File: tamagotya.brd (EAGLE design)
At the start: 27.9 x 31.8 mm, 34 parts, among them U100 ESP32-D2WD, U200 UT-0206-P05FOLDED, U300 4MB Flash, Y100 40Mhz 3.2X2.5

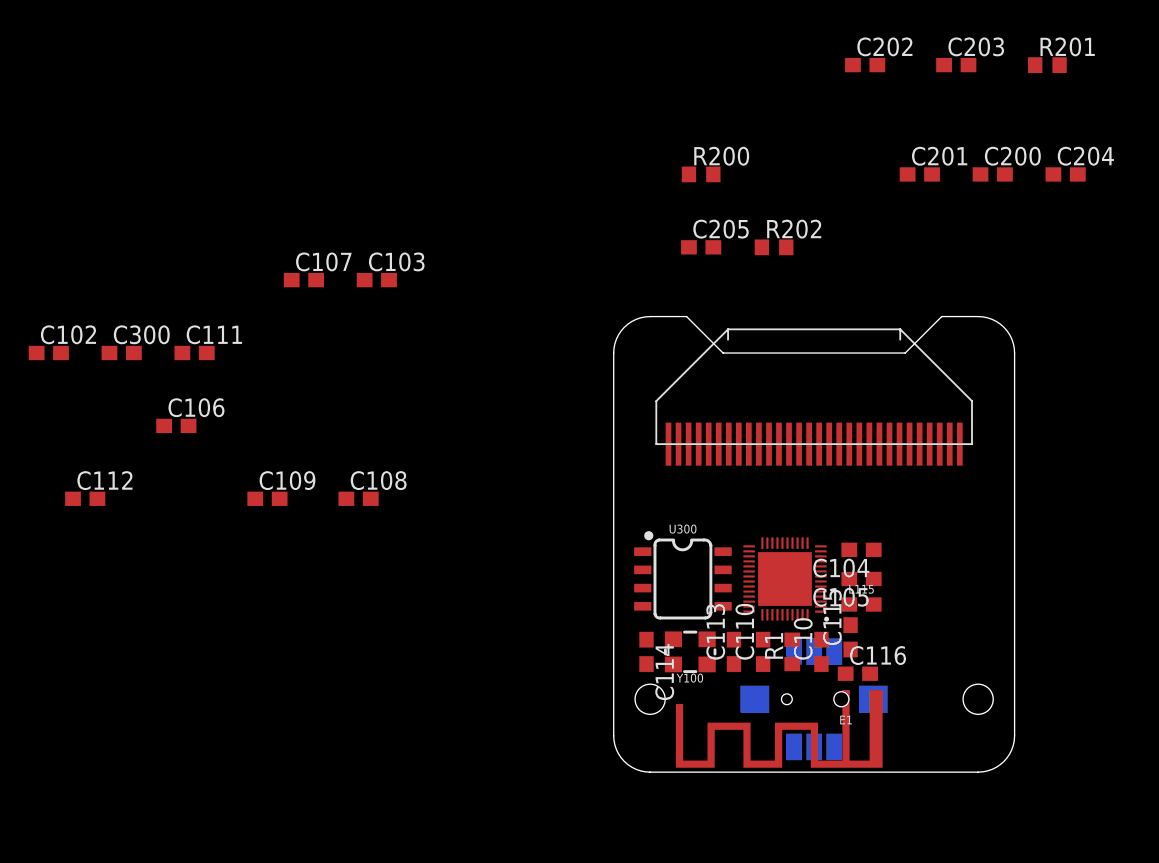
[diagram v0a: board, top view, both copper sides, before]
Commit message: Laid out, need to add charge/boost circuit and its basically done. Could do with a UART too.
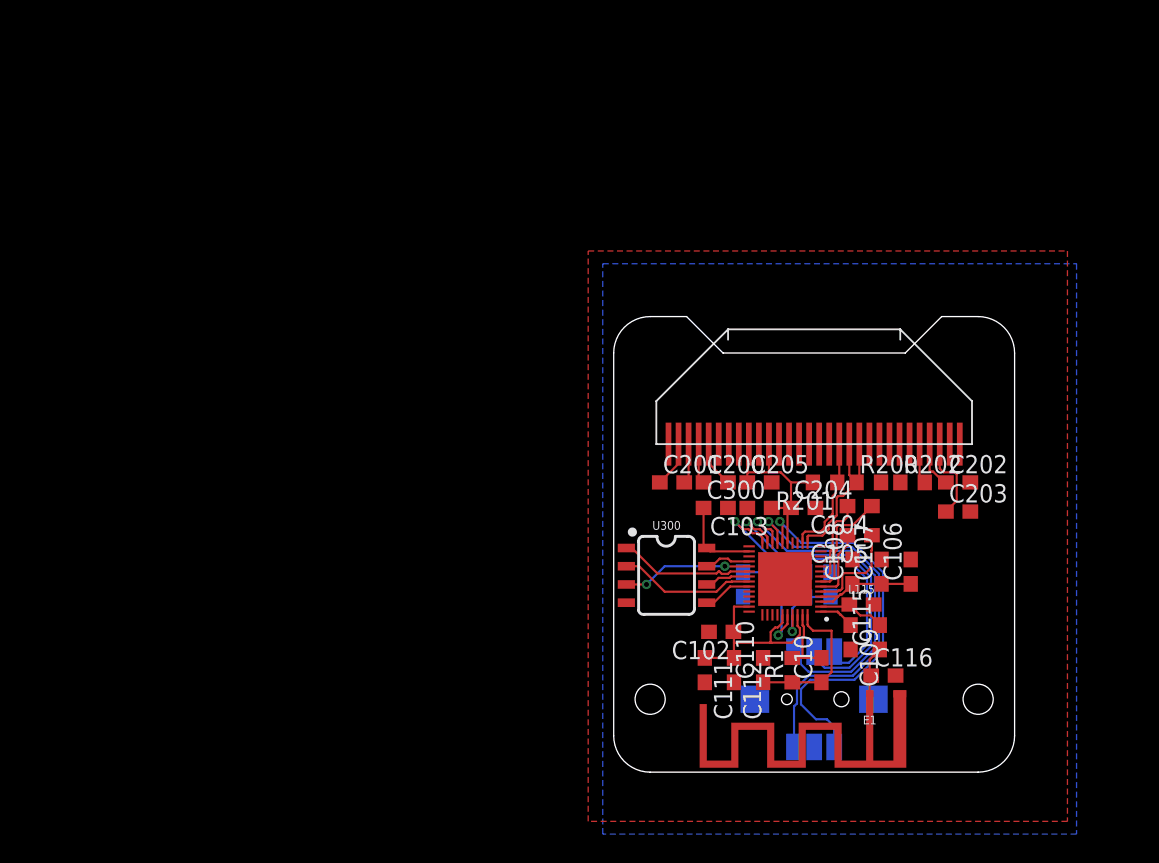
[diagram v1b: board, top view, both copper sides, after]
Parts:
- moved C106 52.2 mm to (20.7, 14.0), turned to 90 degrees
- moved C102 50.7 mm to (7.49, 9.78), turned to 180 degrees
- moved C112 46.8 mm to (8.38, 7.11), turned to 270 degrees
- moved C107 45.1 mm to (18.7, 14.0), turned to 90 degrees
- moved C300 42.8 mm to (7.11, 18.4)
- moved C111 41.9 mm to (6.35, 7.11), turned to 270 degrees
- moved C109 41.8 mm to (16.5, 9.40), turned to 270 degrees
- moved C108 34.8 mm to (16.6, 14.0), turned to 90 degrees
- moved R201 33.0 mm to (14.7, 20.2), turned to 180 degrees
- moved C203 31.1 mm to (24.0, 18.2)
- moved C103 31.0 mm to (10.2, 18.4), turned to 180 degrees
- moved C202 29.8 mm to (24.0, 20.2)
- moved C204 29.6 mm to (13.2, 18.4)
- moved C200 28.9 mm to (7.11, 20.2)
- moved C201 27.5 mm to (4.06, 20.2)
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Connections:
- net N$1 renamed SENSOR_VN
- net N$2 renamed SENSOR_CAPN
- net N$3 renamed SENSOR_VP
- net N$4 renamed SENSOR_CAPP
- net N$8 renamed CAP1
- net N$9 renamed CAP2
- removed net CLICK: JOY.CTR
- removed net DOWN: JOY.D
- removed net GPIO26: U100.15
- removed net GPIO27: U100.16
- removed net LEFT: JOY.C
- removed net RIGHT: JOY.B
- removed net UP: JOY.A
- new net GPIO15: JOY.B, U100.21
- net GPIO0: now also JOY.CTR
- net GPIO13: now also JOY.D
- net GPIO14: no longer U100.21
- net GPIO2: now also JOY.A
- net GPIO4: now also JOY.C
- net SCL: now also U100.16
- net SDA: now also U100.15
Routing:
- net 3.3V: track 0.00 -> 41.0 mm
- net GPIO13: track 0.00 -> 28.0 mm, vias 0 -> 1
- net GPIO15: track 0.00 -> 27.3 mm, vias 0 -> 1
- net GPIO2: track 0.00 -> 24.1 mm, vias 0 -> 1
- net GPIO0: track 0.00 -> 22.8 mm, vias 0 -> 1
- net GPIO4: track 0.00 -> 21.8 mm, vias 0 -> 1
- net SDA: track 0.00 -> 12.1 mm
- net CAP1: track 0.00 -> 10.5 mm
- net SDO/SD0: track 0.00 -> 9.59 mm
- net SCS/CMD: track 0.00 -> 9.49 mm
- net SWP/SD3: track 0.00 -> 9.09 mm, vias 0 -> 2
- net SCL: track 0.00 -> 8.60 mm
- net N$6: track 0.00 -> 8.40 mm, vias 0 -> 1
- net SENSOR_CAPN: track 0.00 -> 7.69 mm
- net SENSOR_VP: track 0.00 -> 7.02 mm
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- added copper zone on layer 1, net GND
- added copper zone on layer 16, net GND
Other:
- board text added: "28mm"
- board text added: "32mm"

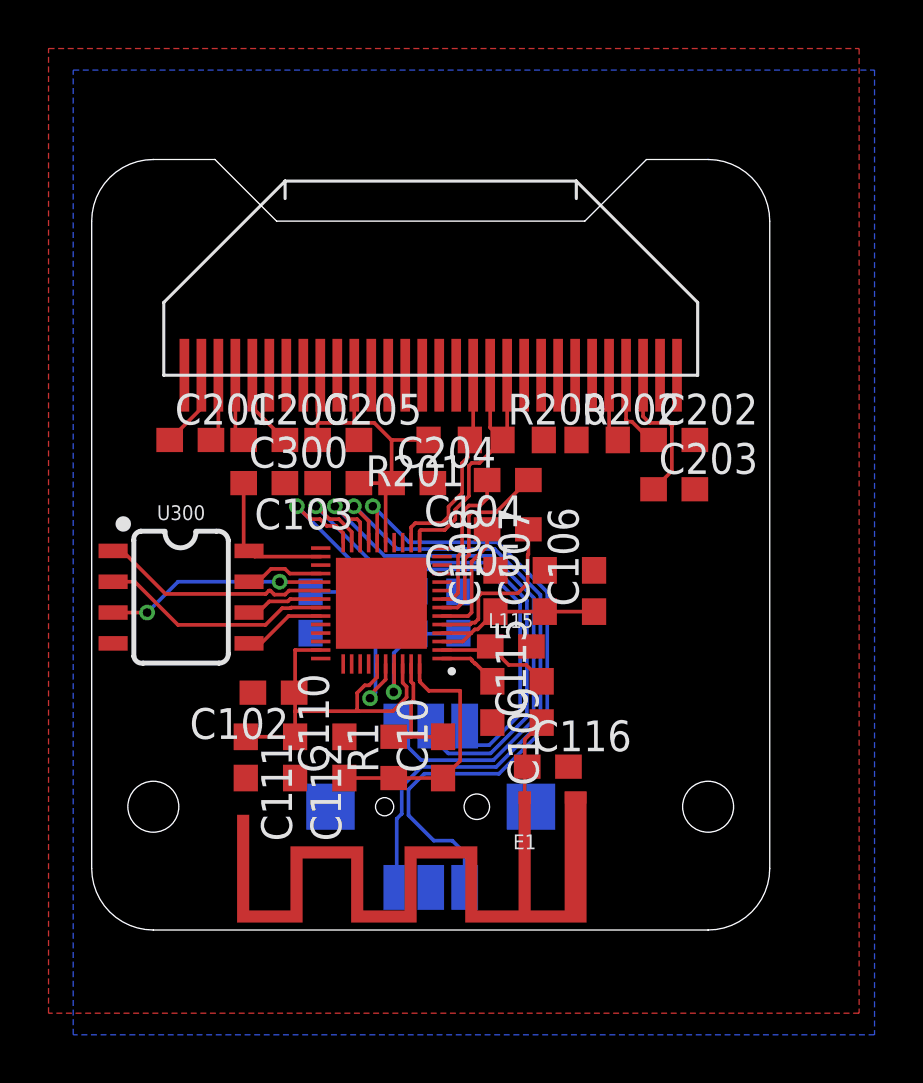
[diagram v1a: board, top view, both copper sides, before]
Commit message: Almost there. Mostly laid out. Just got CP2102 power to resolve.
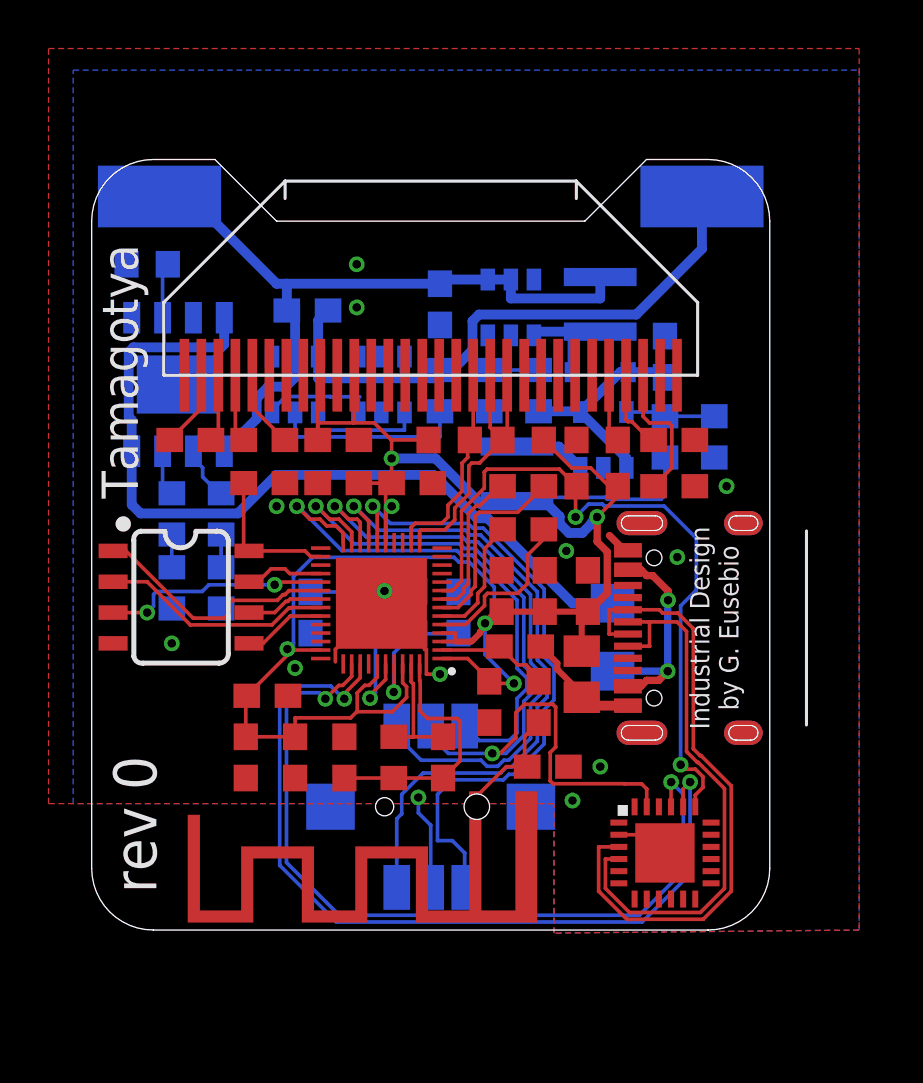
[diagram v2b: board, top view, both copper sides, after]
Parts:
- added C1, C2: 22uH, rcl:C0603
- added C1503: 0.1uF, rcl:C0603
- added C3: 47uF, rcl:C0805
- added D2002: (no value), SparkFun-DiscreteSemi:SOD-323
- added F1: 6V/0.5A, SparkFun-Fuses:1206
- added L2000: 10uH, geusebio:INDUCTOR_3.0X3.0
- added L2100: 4.7uH, geusebio:INDUCTOR_3.0X3.0
- added NEG, POS: (no value), wirepad:SMD2,54-5,08
- added R1001: 1.2k, rcl:R0603
- added R1006, R1007, R1501, R2005, R2103: 1k, rcl:R0603
- added R1008, R1009: 2k, rcl:R0603
- added R2: 10k, rcl:R0603
- added R2004: 7.5k, rcl:R0603
- added R2102: 4.5k, rcl:R0603
- added U$2: USB-C, geusebio:USB_C-XKBENTERPRISEU262-16XN-4BVC11
- added U$3: CP2102N-QFN24, geusebio:QFN24-4X4
- added U1000: TP4056, geusebio:SOP-8
- added U1500: FS312F-G, geusebio:SOT23-6
- added U1550: FS8205, geusebio:SOT23-6
- added U2000: MT3608, geusebio:SOT23-6
- added U2100: M3406, geusebio:SOT23-5
- moved E1 2.03 mm to (15.8, 5.21)
- moved C104 0.68 mm to (17.8, 18.3)
- moved C105 0.64 mm to (17.8, 16.5)
- moved L115 0.38 mm to (17.7, 11.7)
- moved C102 0.28 mm to (7.24, 9.65), turned to 0 degrees
- moved C106 0.25 mm to (20.4, 14.0)
- moved C108 0.25 mm to (16.9, 14.0)
- moved C109 0.13 mm to (16.4, 9.40)
- moved C115 0.13 mm to (18.4, 9.40)
- moved C203 0.13 mm to (24.0, 18.3)
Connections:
- net N$5 renamed XTAL_P
- net N$6 renamed XTAN_N
- removed net CHIP_PU: U100.9
- removed net U0RXD: U100.40
- removed net U0TXD: U100.41
- new net 5V: C2.1, D2002.C, R2004.2, U2100.1, U2100.4
- new net BUCK: D2002.A, L2000.P$2, U2000.1
- new net CHRG: R1006.2, U1000.7
- new net CHRG_3V3: R1006.1, R1008.2
- new net D+: U$2.D+1, U$2.D+2, U$3.3
- new net D-: U$2.D-1, U$2.D-2, U$3.4
- new net FS_CS: R1501.2, U1500.2
- new net GND_BATT: C1503.2, NEG.1, R1501.1, U1500.6, U1550.3
- new net N$17: U$3.5
- new net N$18: U$3.6
- new net N$20: U$3.1
- new net N$21: U$3.24
- new net N$23: U$3.22
- new net N$26: U$3.18
- new net N$27: U$3.17
- new net N$28: U$3.15
- new net N$29: U$3.14
- new net N$3: R2004.1, R2005.2, U2000.3
- new net N$30: U$3.13
- new net N$31: U$3.12
- new net N$32: U$3.11
- new net N$33: U$3.9
- new net N$35: U$3.8
- new net N$36: U$3.7
- new net N$4: R1001.2, U1000.2
- new net N$8: L2100.P$1, U2100.3
- new net N$9: R2102.1, R2103.2, U2100.5
- new net OC: U1500.3, U1550.6
- new net OD: U1500.1, U1550.4
- new net RESET: R2.1, U$3.19, U100.9
- new net STDBY: R1007.2, U1000.6
- new net STDBY_3V3: R1007.1, R1009.2
- new net U100RXD: U$3.21, U100.40
- new net U100TXD: U$3.20, U100.41
- new net V_BATT: C1.1, C1503.1, L2000.P$1, POS.1, U1000.5, U1500.5, U2000.4, U2000.5
- new net V_USB: F1.1, U1000.4, U1000.8
- new net V_USB_UNFUSED: F1.2, U$2.V+1, U$2.V+2
- net 3.3V: now also C3.1, L2100.P$2, R2.2, R2102.2
- net GND: now also C1.2, C2.2, C3.2, R1001.1, R1008.1, R1009.1, R2005.1, R2103.1, U$2.GND1, U$2.GND2, U$3.2, U$3.EXP, U1000.1, U1000.3, U1550.1, U2000.2, U2100.2
- net GPIO0: now also U$3.23
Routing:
- net 3.3V: track 41.0 -> 93.3 mm, vias 0 -> 6
- net U100TXD: track 0.00 -> 35.2 mm, vias 0 -> 2
- net V_USB: track 0.00 -> 34.7 mm
- net U100RXD: track 0.00 -> 33.3 mm, vias 0 -> 2
- net V_BATT: track 0.00 -> 30.7 mm
- net RESET: track 0.00 -> 29.2 mm, vias 0 -> 2
- net D+: track 0.00 -> 26.1 mm
- net GND_BATT: track 0.00 -> 24.9 mm
- net D-: track 0.00 -> 23.5 mm
- net GND: track 0.00 -> 21.4 mm, vias 0 -> 13
- net GPIO0: track 22.8 -> 35.4 mm, vias 1 -> 2
- net V_USB_UNFUSED: track 0.00 -> 9.52 mm, vias 0 -> 2
- net 5V: track 0.00 -> 9.08 mm
- net FS_CS: track 0.00 -> 8.03 mm
- net OD: track 0.00 -> 5.02 mm
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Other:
- board text added: "+"
- board text added: "-"
- board text added: "Industrial Design by G. Eusebio"
- board text added: "Tamagotya"
- board text added: "rev 0"

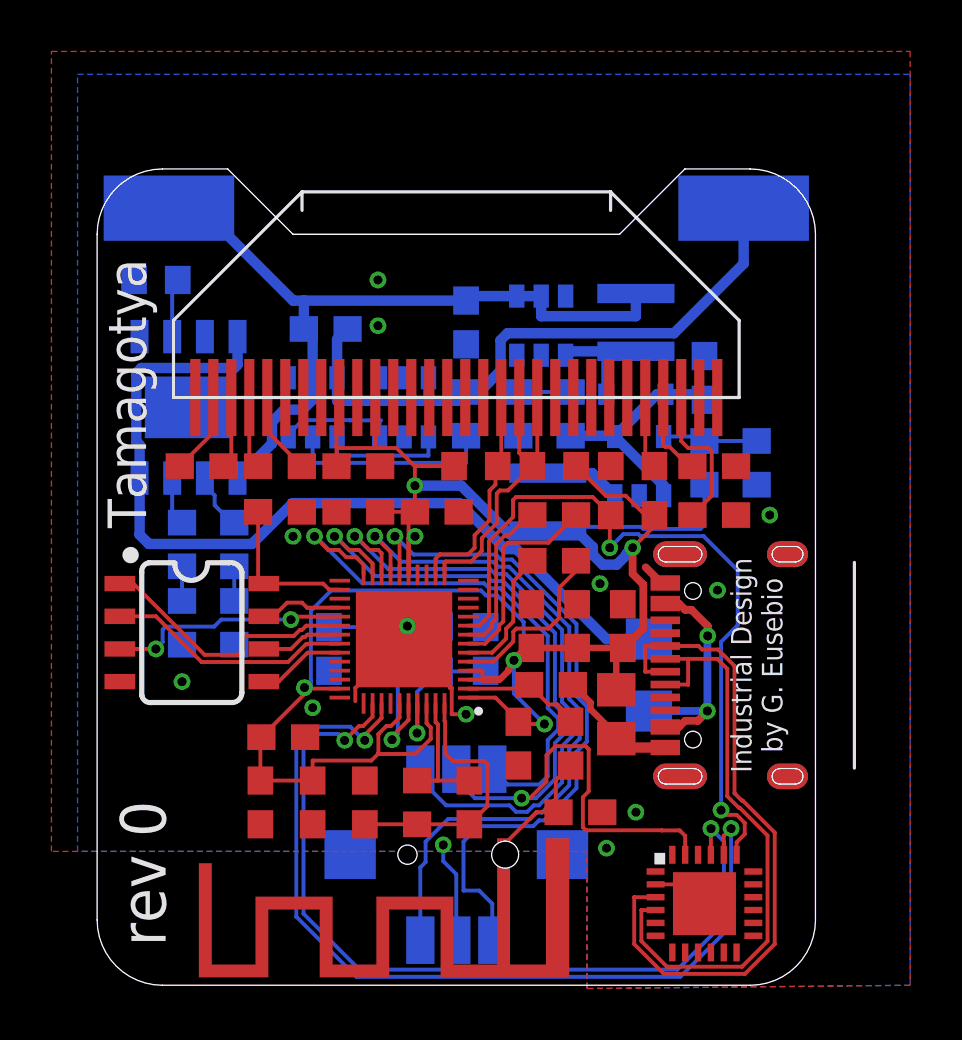
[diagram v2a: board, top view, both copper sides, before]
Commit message: CP2102 now has adequate power circuitry, I believe
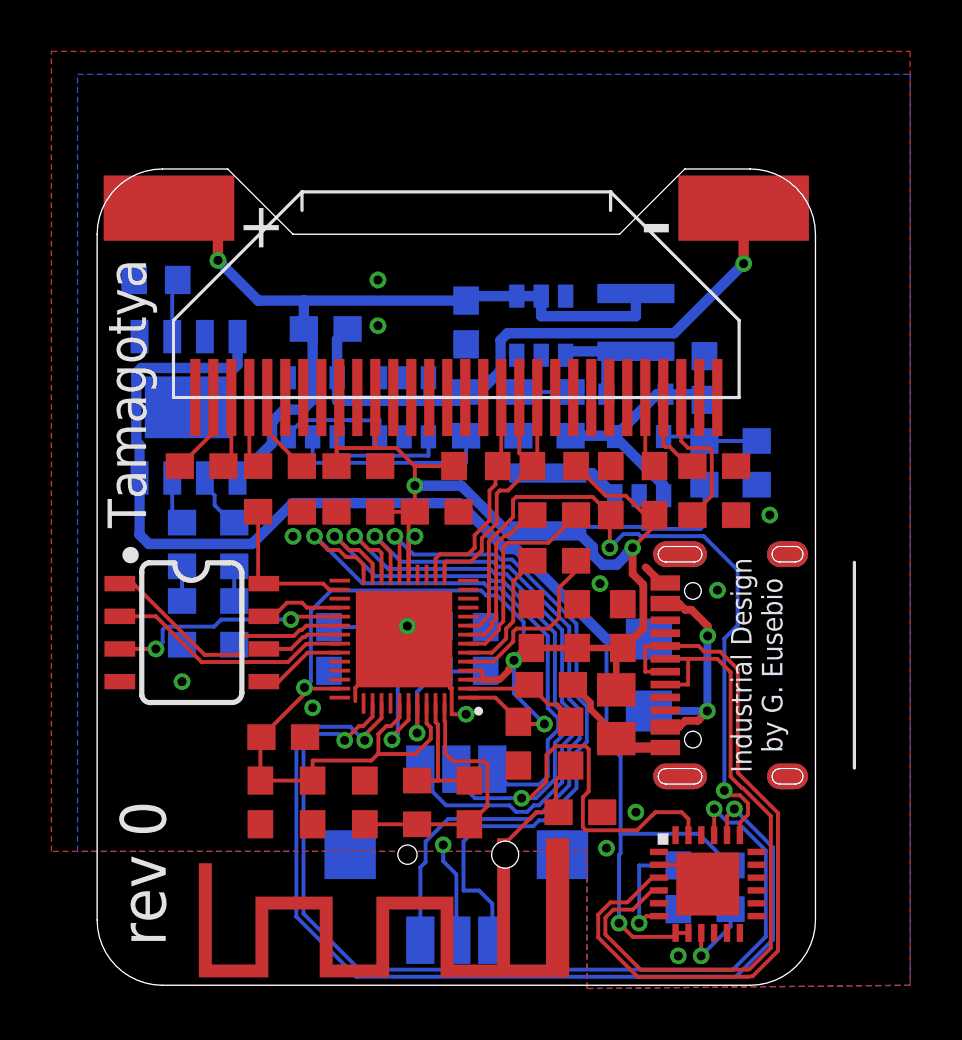
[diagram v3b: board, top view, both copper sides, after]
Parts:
- added C4: 0.1uF, rcl:C0603
- added R3: 4.7k, rcl:R0603
- moved U$3 0.77 mm to (23.7, 3.94)
- flipped NEG to the top
- flipped POS to the top
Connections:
- removed net N$18: U$3.6
- removed net N$33: U$3.9
- removed net N$35: U$3.8
- removed net N$36: U$3.7
- new net CP3V3: C4.1, U$3.6
- new net CPRST: R3.1, U$3.9
- net GND: now also C4.2
- net V_USB: now also R3.2, U$3.7, U$3.8
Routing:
- net V_USB: track 34.7 -> 53.5 mm, vias 0 -> 1
- net CP3V3: track 0.00 -> 4.65 mm, vias 0 -> 1
- net U100RXD: track 33.3 -> 36.9 mm
- net U100TXD: track 35.2 -> 38.5 mm
- net CPRST: track 0.00 -> 3.19 mm, vias 0 -> 1
- net D+: track 26.1 -> 29.2 mm
- net D-: track 23.5 -> 26.6 mm
- net 3.3V: track 93.3 -> 91.9 mm
- net V_BATT: track 30.7 -> 31.6 mm, vias 0 -> 1
- net RESET: track 29.2 -> 28.3 mm
- net GND: track 21.4 -> 21.5 mm, vias 13 -> 14
- net GND_BATT: vias 0 -> 1
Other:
- board text added: "TODO: ADC sensing battery voltage. DAC output for small speaker ESP32 TX/RX/RST/GPIO-0 breakout Accellerometer would be reet grand I2C breakout?"
